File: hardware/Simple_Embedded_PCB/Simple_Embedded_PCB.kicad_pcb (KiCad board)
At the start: 4 copper layers, 74.9 x 58.5 mm, 66 parts, among them J1 USB_B_Micro, J2 SWD Connector, J3 Conn_01x09, J4 Conn_01x09, J5 Conn_01x09, J6 Conn_01x09, J7 5.5mm X 2.1mm Jack, Q1 AO3400A, Q2 AO3401A, U1 STM32F103C8Tx, U2 LMR16020PDDA, U3 AMS1117-3.3, X1 SG-8018CE 8.000000MHz

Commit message: Added JLCPCB part numbers
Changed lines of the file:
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@@
       (layerselection 0x00010fc_ffffffff)
       (disableapertmacros false)
-      (usegerberextensions false)
-      (usegerberattributes true)
-      (usegerberadvancedattributes true)
-      (creategerberjobfile true)
+      (usegerberextensions true)
+      (usegerberattributes false)
+      (usegerberadvancedattributes false)
+      (creategerberjobfile false)
       (svguseinch false)
       (svgprecision 6)
@@
       (psa4output false)
       (plotreference true)
-      (plotvalue true)
+      (plotvalue false)
       (plotinvisibletext false)
       (sketchpadsonfab false)
-      (subtractmaskfromsilk false)
+      (subtractmaskfromsilk true)
       (outputformat 1)
       (mirror false)
-      (drillshape 1)
+      (drillshape 0)
       (scaleselection 1)
-      (outputdirectory "")
+      (outputdirectory "gerber/")
     )
   )
@@
     (fp_line (start 1.6 -0.8) (end 1.6 0.8) (layer "F.Fab") (width 0.1))
     (fp_line (start -1.6 -0.8) (end 1.6 -0.8) (layer "F.Fab") (width 0.1))
-    (pad "1" smd roundrect (at -1.475 0 270) (size 1.15 1.8) (layers "F.Cu" "F.Paste" "F.Mask") (roundrect_rratio 0.217391)
+    (pad "1" smd roundrect (at -1.475 0 270) (size 1.15 1.8) (layers "F.Cu" "F.Paste" "F.Mask") (roundrect_rratio 0.2173913043)
       (net 1 "+3.3V") (pintype "passive"))
-    (pad "2" smd roundrect (at 1.475 0 270) (size 1.15 1.8) (layers "F.Cu" "F.Paste" "F.Mask") (roundrect_rratio 0.217391)
+    (pad "2" smd roundrect (at 1.475 0 270) (size 1.15 1.8) (layers "F.Cu" "F.Paste" "F.Mask") (roundrect_rratio 0.2173913043)
       (net 8 "Net-(C18-Pad2)") (pintype "passive"))
     (model "${KICAD6_3DMODEL_DIR}/Capacitor_SMD.3dshapes/C_1206_3216Metric.wrl"
@@
     (fp_line (start -1.6 -0.8) (end 1.6 -0.8) (layer "F.Fab") (width 0.1))
     (fp_line (start 1.6 -0.8) (end 1.6 0.8) (layer "F.Fab") (width 0.1))
-    (pad "1" smd roundrect (at -1.475 0 270) (size 1.15 1.8) (layers "F.Cu" "F.Paste" "F.Mask") (roundrect_rratio 0.217391)
+    (pad "1" smd roundrect (at -1.475 0 270) (size 1.15 1.8) (layers "F.Cu" "F.Paste" "F.Mask") (roundrect_rratio 0.2173913043)
       (net 1 "+3.3V") (pintype "passive"))
-    (pad "2" smd roundrect (at 1.475 0 270) (size 1.15 1.8) (layers "F.Cu" "F.Paste" "F.Mask") (roundrect_rratio 0.217391)
+    (pad "2" smd roundrect (at 1.475 0 270) (size 1.15 1.8) (layers "F.Cu" "F.Paste" "F.Mask") (roundrect_rratio 0.2173913043)
       (net 9 "Net-(C20-Pad2)") (pintype "passive"))
     (model "${KICAD6_3DMODEL_DIR}/Capacitor_SMD.3dshapes/C_1206_3216Metric.wrl"
@@
     (fp_line (start -1.6 -0.8) (end 1.6 -0.8) (layer "F.Fab") (width 0.1))
     (fp_line (start -1.6 0.8) (end -1.6 -0.8) (layer "F.Fab") (width 0.1))
-    (pad "1" smd roundrect (at -1.475 0 90) (size 1.15 1.8) (layers "F.Cu" "F.Paste" "F.Mask") (roundrect_rratio 0.217391)
+    (pad "1" smd roundrect (at -1.475 0 90) (size 1.15 1.8) (layers "F.Cu" "F.Paste" "F.Mask") (roundrect_rratio 0.2173913043)
       (net 3 "+12V") (pintype "passive"))
-    (pad "2" smd roundrect (at 1.475 0 90) (size 1.15 1.8) (layers "F.Cu" "F.Paste" "F.Mask") (roundrect_rratio 0.217391)
+    (pad "2" smd roundrect (at 1.475 0 90) (size 1.15 1.8) (layers "F.Cu" "F.Paste" "F.Mask") (roundrect_rratio 0.2173913043)
       (net 2 "GND") (pintype "passive"))
     (model "${KICAD6_3DMODEL_DIR}/Capacitor_SMD.3dshapes/C_1206_3216Metric.wrl"
@@
     (fp_line (start 1.6 -0.8) (end 1.6 0.8) (layer "F.Fab") (width 0.1))
     (fp_line (start 1.6 0.8) (end -1.6 0.8) (layer "F.Fab") (width 0.1))
-    (pad "1" smd roundrect (at -1.475 0 90) (size 1.15 1.8) (layers "F.Cu" "F.Paste" "F.Mask") (roundrect_rratio 0.217391)
+    (pad "1" smd roundrect (at -1.475 0 90) (size 1.15 1.8) (layers "F.Cu" "F.Paste" "F.Mask") (roundrect_rratio 0.2173913043)
       (net 3 "+12V") (pintype "passive"))
-    (pad "2" smd roundrect (at 1.475 0 90) (size 1.15 1.8) (layers "F.Cu" "F.Paste" "F.Mask") (roundrect_rratio 0.217391)
+    (pad "2" smd roundrect (at 1.475 0 90) (size 1.15 1.8) (layers "F.Cu" "F.Paste" "F.Mask") (roundrect_rratio 0.2173913043)
       (net 2 "GND") (pintype "passive"))
     (model "${KICAD6_3DMODEL_DIR}/Capacitor_SMD.3dshapes/C_1206_3216Metric.wrl"
@@
     (fp_line (start -1.6 0.8) (end -1.6 -0.8) (layer "F.Fab") (width 0.1))
     (fp_line (start -1.6 -0.8) (end 1.6 -0.8) (layer "F.Fab") (width 0.1))
-    (pad "1" smd roundrect (at -1.475 0 270) (size 1.15 1.8) (layers "F.Cu" "F.Paste" "F.Mask") (roundrect_rratio 0.217391)
+    (pad "1" smd roundrect (at -1.475 0 270) (size 1.15 1.8) (layers "F.Cu" "F.Paste" "F.Mask") (roundrect_rratio 0.2173913043)
       (net 4 "+5V") (pintype "passive"))
-    (pad "2" smd roundrect (at 1.475 0 270) (size 1.15 1.8) (layers "F.Cu" "F.Paste" "F.Mask") (roundrect_rratio 0.217391)
+    (pad "2" smd roundrect (at 1.475 0 270) (size 1.15 1.8) (layers "F.Cu" "F.Paste" "F.Mask") (roundrect_rratio 0.2173913043)
       (net 2 "GND") (pintype "passive"))
     (model "${KICAD6_3DMODEL_DIR}/Capacitor_SMD.3dshapes/C_1206_3216Metric.wrl"
@@
     (fp_line (start 1.6 -0.8) (end 1.6 0.8) (layer "F.Fab") (width 0.1))
     (fp_line (start 1.6 0.8) (end -1.6 0.8) (layer "F.Fab") (width 0.1))
-    (pad "1" smd roundrect (at -1.475 0 270) (size 1.15 1.8) (layers "F.Cu" "F.Paste" "F.Mask") (roundrect_rratio 0.217391)
+    (pad "1" smd roundrect (at -1.475 0 270) (size 1.15 1.8) (layers "F.Cu" "F.Paste" "F.Mask") (roundrect_rratio 0.2173913043)
       (net 4 "+5V") (pintype "passive"))
-    (pad "2" smd roundrect (at 1.475 0 270) (size 1.15 1.8) (layers "F.Cu" "F.Paste" "F.Mask") (roundrect_rratio 0.217391)
+    (pad "2" smd roundrect (at 1.475 0 270) (size 1.15 1.8) (layers "F.Cu" "F.Paste" "F.Mask") (roundrect_rratio 0.2173913043)
       (net 2 "GND") (pintype "passive"))
     (model "${KICAD6_3DMODEL_DIR}/Capacitor_SMD.3dshapes/C_1206_3216Metric.wrl"

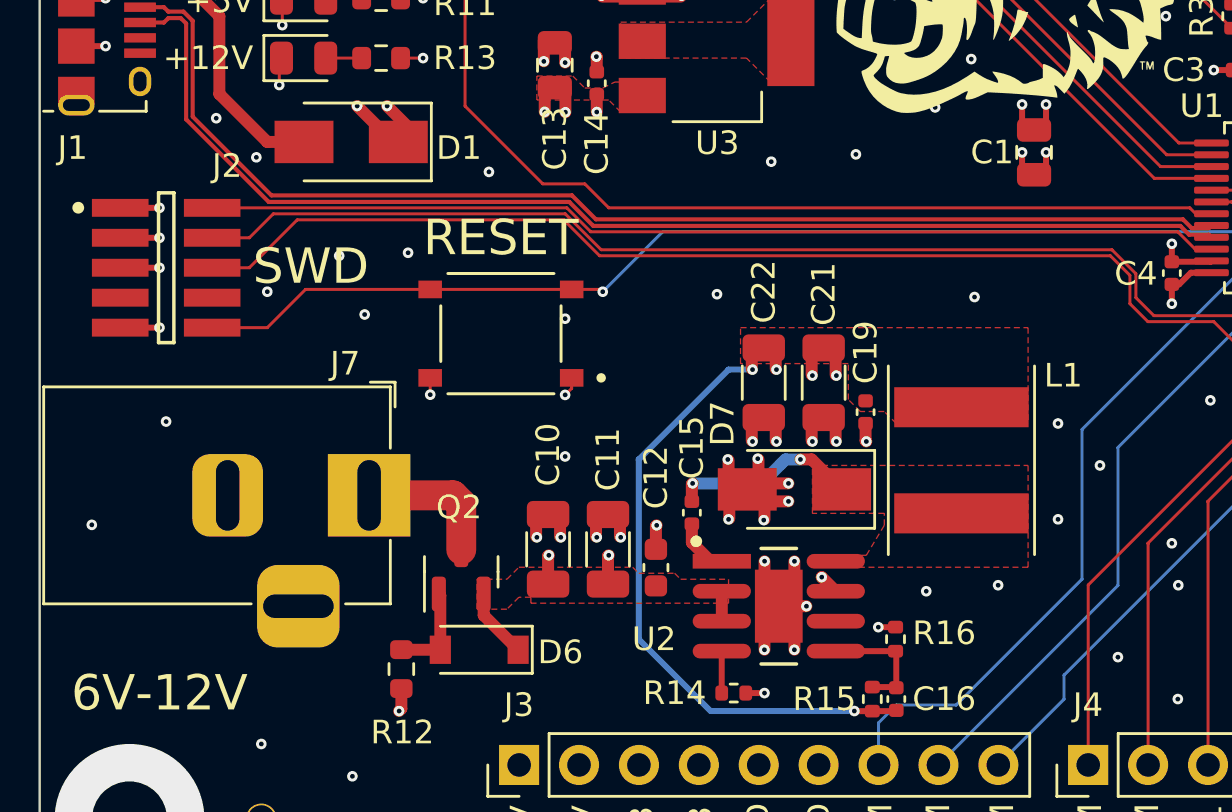
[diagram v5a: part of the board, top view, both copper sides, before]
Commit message: Changed KiCad project to use symbols, footprints, and 3D models from project itself.
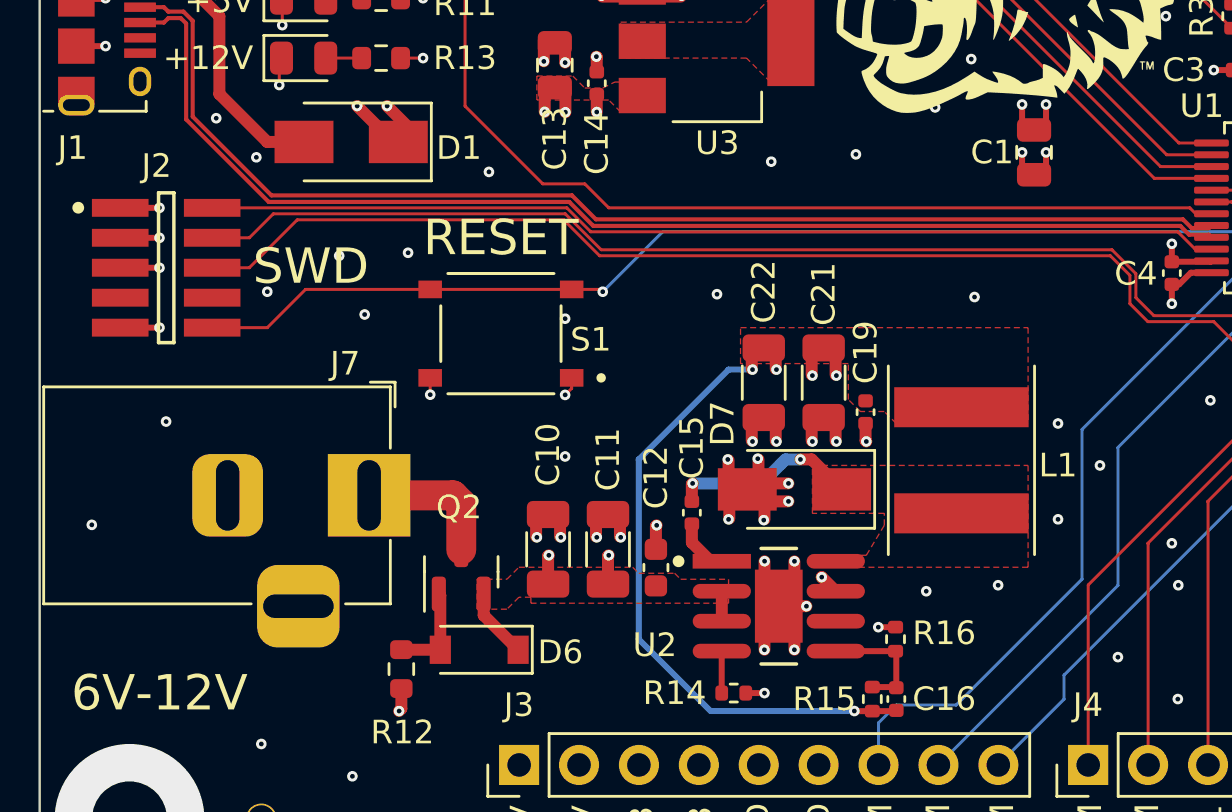
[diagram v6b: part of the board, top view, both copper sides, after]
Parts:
- H1, H2, H3: footprint MySO:ToolingHole_JLCPCB -> Simple_Embedded_PCB:ToolingHole_JLCPCB
- J2: footprint MySO:Amphenol-20021121-0-0-0 -> Simple_Embedded_PCB:Amphenol-20021121-0-0-0
- L1: footprint MySO:SUNLORD_SWPA6045S4R7MT -> Simple_Embedded_PCB:SUNLORD_SWPA6045S4R7MT
- S1: footprint MySO:SW_TS-1187A-B-A-B -> Simple_Embedded_PCB:SW_TS-1187A-B-A-B
- U2: footprint MySO:8-PowerSOIC -> Simple_Embedded_PCB:8-PowerSOIC
